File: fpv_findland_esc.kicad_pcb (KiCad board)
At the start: 6 copper layers, 36 x 47.4 mm, 157 parts, among them J1 Conn_01x01_Pin, J10 Conn_01x01_Pin, J11 Conn_01x01_Pin, J12 Conn_01x01_Pin, J13 Conn_01x06, J2 Conn_01x01_Pin, J3 Conn_01x01_Pin, J4 Conn_01x01_Pin, J5 Conn_01x01_Pin, J6 Conn_01x01_Pin, J7 Conn_01x01_Pin, J8 Conn_01x01_Pin, J9 Conn_01x01_Pin, Q1 FDMC8010DC, Q10 FDMC8010DC, Q11 FDMC8010DC, Q12 FDMC8010DC, Q13 FDMC8010DC, Q14 FDMC8010DC, Q15 FDMC8010DC, Q16 FDMC8010DC, Q17 FDMC8010DC, Q18 FDMC8010DC, Q19 FDMC8010DC, Q2 FDMC8010DC, Q20 FDMC8010DC, Q21 FDMC8010DC, Q22 FDMC8010DC, Q23 FDMC8010DC, Q24 FDMC8010DC, Q3 FDMC8010DC, Q4 FDMC8010DC, Q5 FDMC8010DC, Q6 FDMC8010DC, Q7 FDMC8010DC, Q8 FDMC8010DC, Q9 FDMC8010DC, U1 GD32E230G8U6, U11 WL2851E33, U2 DRV8300D, U3 GD32E230G8U6, U4 DRV8300D, U5 GD32E230G8U6, U6 DRV8300D, U7 GD32E230G8U6, U8 DRV8300D, U9 ST732M50R

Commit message: Fixed revisions
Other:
- board text added: "${revision}"

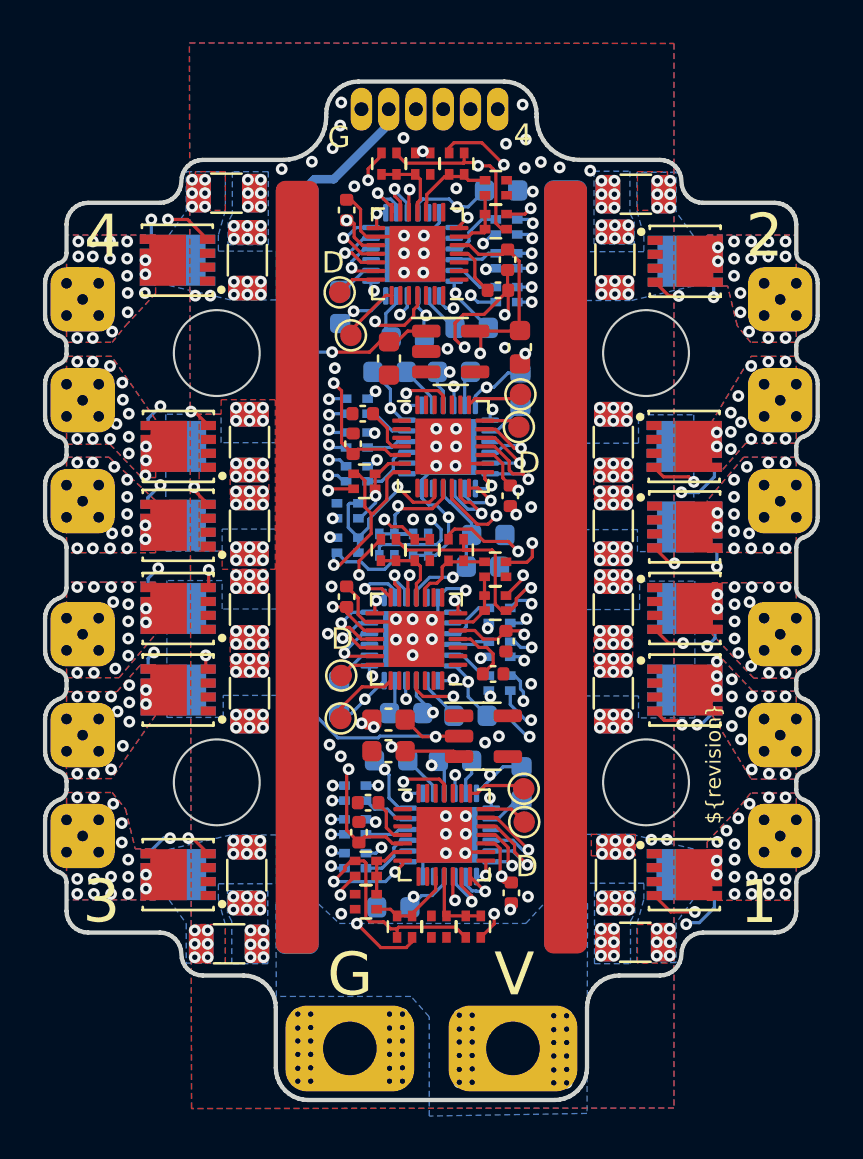
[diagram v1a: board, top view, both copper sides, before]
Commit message: Added copperfill for VBAT in layer In4. Other small fixes.
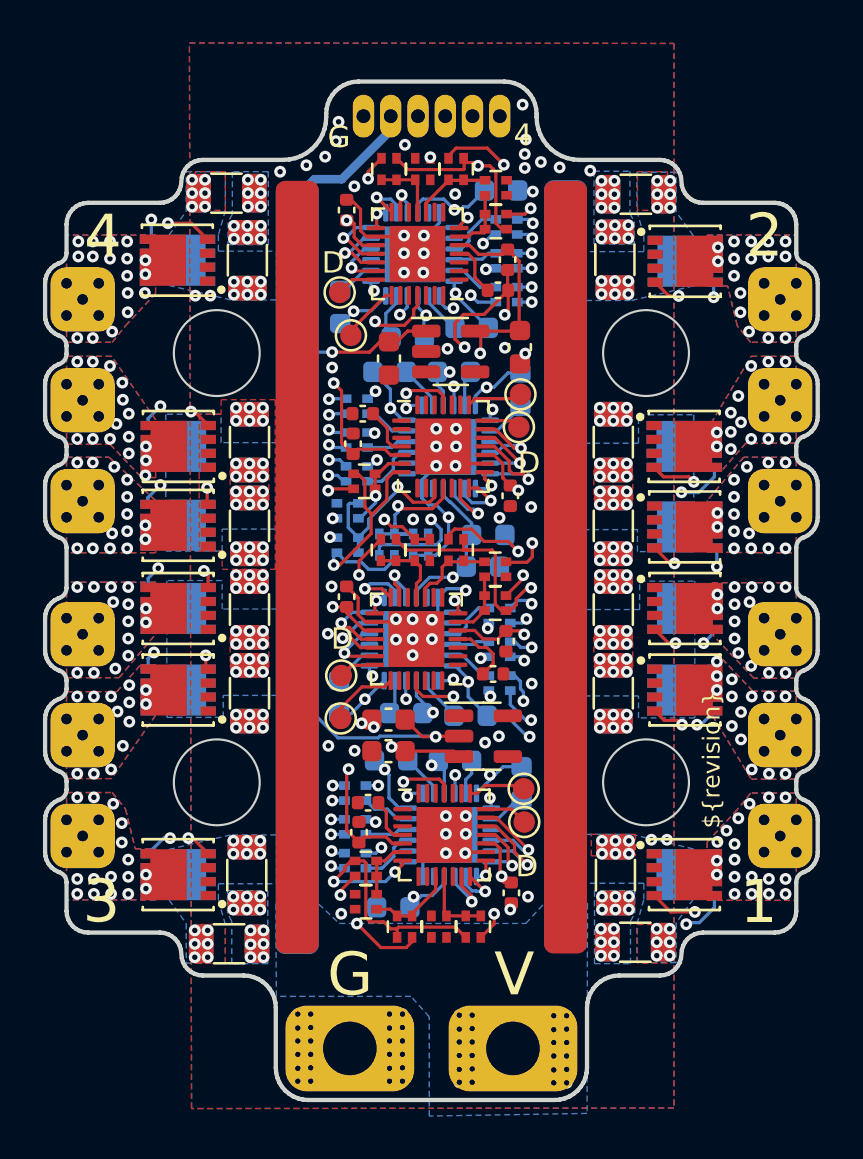
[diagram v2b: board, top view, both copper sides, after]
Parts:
- moved J13 0.34 mm to (138.7, 54.0)
- moved RN24 0.25 mm to (136.7, 56.4)
- moved RN20 0.25 mm to (133.5, 56.4)
- moved RN21 0.25 mm to (135.1, 56.4)
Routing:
- net /VBAT: track 79.7 -> 90.8 mm
- net /Motor2/V_SENSE: track 3.24 -> 0.00 mm, vias 1 -> 0
- net /3.3V: track 99.9 -> 102.8 mm
- net /Motor1/V_SENSE: track 1.15 -> 0.00 mm, vias 1 -> 0
- net /Motor4/V_SENSE: track 1.08 -> 0.00 mm, vias 1 -> 0
- net /Motor3/V_SENSE: track 1.07 -> 0.00 mm, vias 1 -> 0
- net /Motor3/CLOW: track 2.55 -> 1.76 mm
- net Net-(Q24-G): track 10.6 -> 9.89 mm
- added copper zone on In2.Cu, net /VBAT

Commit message: Optimized layer In2 for more current.
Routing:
- net /5V: track 75.2 -> 73.8 mm
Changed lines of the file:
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@@
   (via (at 133.646479 83.347485) (size 0.55) (drill 0.25) (layers "F.Cu" "B.Cu") (net 196))
   (segment (start 136.042746 91.7) (end 139.438173 91.7) (width 0.3) (layer "In2.Cu") (net 196))
-  (segment (start 136.4995 75.45) (end 137.425 75.45) (width 0.3) (layer "In2.Cu") (net 196))
+  (segment (start 140.85 73.125) (end 140.85 71.957107) (width 0.3) (layer "In2.Cu") (net 196))
+  (segment (start 140.85 64.25) (end 140.85 71.957107) (width 0.3) (layer "In2.Cu") (net 196))
   (segment (start 140.594655 90.543518) (end 140.594655 84.021695) (width 0.3) (layer "In2.Cu") (net 196))
   (segment (start 135.9149 83.80102) (end 140.37398 83.80102) (width 0.3) (layer "In2.Cu") (net 196))
-  (segment (start 141.325 73.125) (end 141.325 71.482107) (width 0.3) (layer "In2.Cu") (net 196))
   (segment (start 135.733375 83.633375) (end 135.747255 83.633375) (width 0.3) (layer "In2.Cu") (net 196))
+  (segment (start 137.425 75.45) (end 139.75 73.125) (width 0.3) (layer "In2.Cu") (net 196))
   (segment (start 135.747255 83.633375) (end 135.9149 83.80102) (width 0.3) (layer "In2.Cu") (net 196))
+  (segment (start 138.314228 58.114228) (end 139.5 59.3) (width 0.3) (layer "In2.Cu") (net 196))
+  (segment (start 139.5 59.3) (end 139.5 62.9) (width 0.3) (layer "In2.Cu") (net 196))
   (segment (start 136.954592 58.114228) (end 138.314228 58.114228) (width 0.3) (layer "In2.Cu") (net 196))
-  (segment (start 139.75 73.125) (end 141.325 73.125) (width 0.3) (layer "In2.Cu") (net 196))
-  (segment (start 137.425 75.45) (end 139.75 73.125) (width 0.3) (layer "In2.Cu") (net 196))
   (segment (start 140.594655 84.021695) (end 140.37398 83.80102) (width 0.3) (layer "In2.Cu") (net 196))
-  (segment (start 139.5 59.3) (end 139.5 62.9) (width 0.3) (layer "In2.Cu") (net 196))
   (segment (start 134.668246 90.3255) (end 136.042746 91.7) (width 0.3) (layer "In2.Cu") (net 196))
   (segment (start 136.74382 58.325) (end 136.954592 58.114228) (width 0.3) (layer "In2.Cu") (net 196))
-  (segment (start 141.325 71.482107) (end 141.325 82.85) (width 0.3) (layer "In2.Cu") (net 196))
-  (segment (start 141.325 64.725) (end 141.325 71.482107) (width 0.3) (layer "In2.Cu") (net 196))
+  (segment (start 136.5745 58.325) (end 136.74382 58.325) (width 0.3) (layer "In2.Cu") (net 196))
   (segment (start 133.748994 83.45) (end 135.55 83.45) (width 0.3) (layer "In2.Cu") (net 196))
-  (segment (start 139.5 62.9) (end 141.325 64.725) (width 0.3) (layer "In2.Cu") (net 196))
+  (segment (start 139.75 73.125) (end 140.85 73.125) (width 0.3) (layer "In2.Cu") (net 196))
   (segment (start 133.646479 83.347485) (end 133.748994 83.45) (width 0.3) (layer "In2.Cu") (net 196))
-  (segment (start 141.325 82.85) (end 140.37398 83.80102) (width 0.3) (layer "In2.Cu") (net 196))
+  (segment (start 136.4995 75.45) (end 137.425 75.45) (width 0.3) (layer "In2.Cu") (net 196))
+  (segment (start 139.5 62.9) (end 140.85 64.25) (width 0.3) (layer "In2.Cu") (net 196))
+  (segment (start 140.85 83.325) (end 140.37398 83.80102) (width 0.3) (layer "In2.Cu") (net 196))
   (segment (start 135.55 83.45) (end 135.733375 83.633375) (width 0.3) (layer "In2.Cu") (net 196))
-  (segment (start 136.5745 58.325) (end 136.74382 58.325) (width 0.3) (layer "In2.Cu") (net 196))
-  (segment (start 138.314228 58.114228) (end 139.5 59.3) (width 0.3) (layer "In2.Cu") (net 196))
+  (segment (start 140.85 71.957107) (end 140.85 83.325) (width 0.3) (layer "In2.Cu") (net 196))
   (segment (start 139.438173 91.7) (end 140.594655 90.543518) (width 0.3) (layer "In2.Cu") (net 196))
   (segment (start 137.375 72.925) (end 137.375 73.475) (width 0.15) (layer "B.Cu") (net 196))

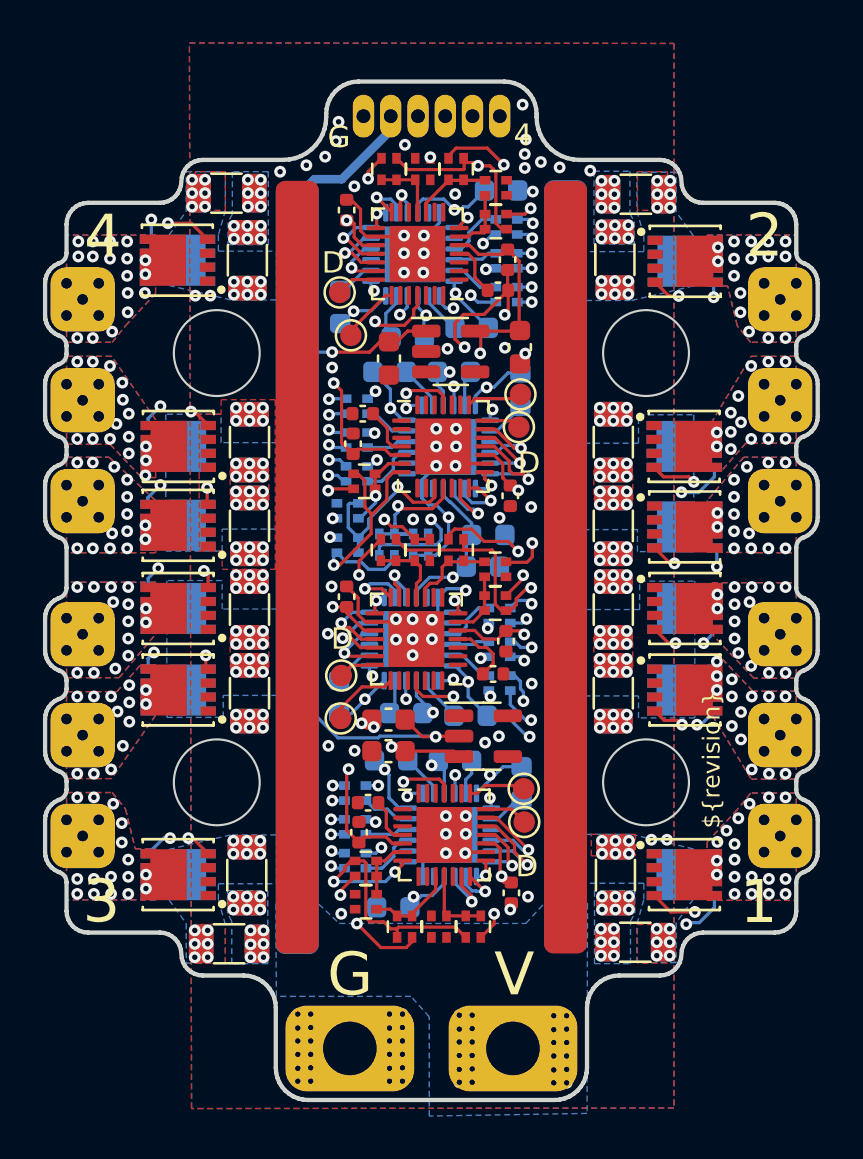
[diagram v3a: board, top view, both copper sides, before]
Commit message: Moved top layer fets to allow more current. Other small improvements.
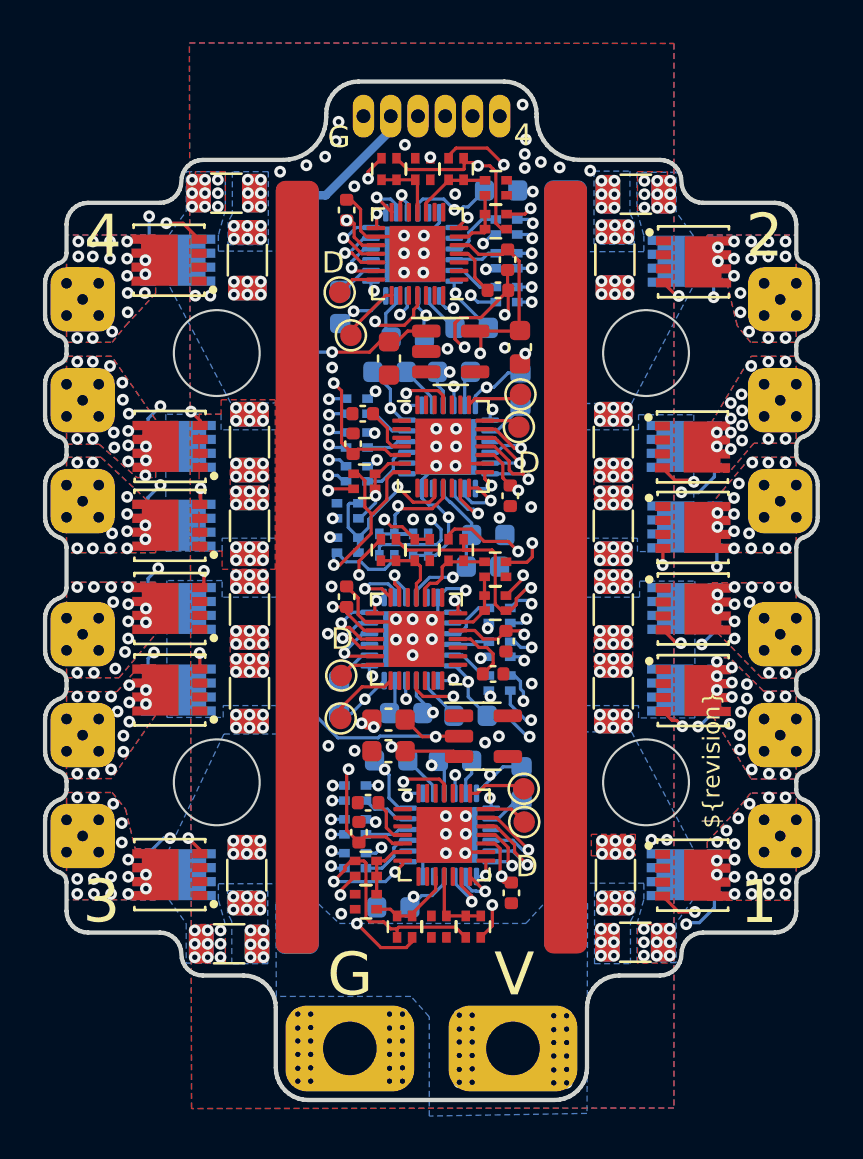
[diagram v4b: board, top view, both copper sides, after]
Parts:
- moved Q12 0.39 mm to (147.7, 89.3)
- moved Q2 0.39 mm to (147.7, 60.8)
- moved Q10 0.39 mm to (147.7, 69.4)
- moved Q7 0.39 mm to (147.7, 73.1)
- moved Q8 0.39 mm to (147.7, 76.9)
- moved Q9 0.39 mm to (147.7, 80.7)
- moved Q11 0.39 mm to (123.3, 89.3)
- moved Q3 0.39 mm to (123.3, 73.0)
- moved Q4 0.39 mm to (123.3, 69.3)
- moved Q5 0.39 mm to (123.3, 80.7)
- moved Q6 0.39 mm to (123.3, 76.9)
- moved Q1 0.39 mm to (123.3, 60.7)
- renumbered C40 to C1, C57 to C10, C64 to C11, C22 to C12, C5 to C13, C4 to C14, C23 to C15, C58 to C16, C30 to C17, C31 to C18, C25 to C19, C38 to C2, C8 to C20, C13 to C21, C29 to C22, C6 to C23, C49 to C24, C50 to C25, C48 to C26, C43 to C27, C1 to C28, C51 to C29, C15 to C3, C53 to C30, C55 to C31, C52 to C32, C69 to C33, C70 to C34, C37 to C35, C19 to C36, C39 to C37, C17 to C38, C45 to C39, C18 to C4, C47 to C40, C46 to C41, C44 to C42, C61 to C43, C60 to C44, C3 to C45, C20 to C46, C62 to C47, C10 to C48, C9 to C49, C16 to C5, C27 to C50, C14 to C51, C7 to C52, C59 to C53, C12 to C54, C26 to C55, C21 to C56, C2 to C57, C28 to C58, C24 to C59, C71 to C6, C66 to C60, C54 to C61, C11 to C62, C67 to C63, C65 to C64, C68 to C7, C63 to C8, C32 to C9, J4 to J1, J8 to J10, J12 to J11, J10 to J12, J11 to J13, J13 to J2, J9 to J3, J6 to J4, J3 to J5, J5 to J6, J1 to J7, J2 to J8, J7 to J9, Q8 to Q1, Q16 to Q10, Q6 to Q11, Q20 to Q12, Q17 to Q13, Q7 to Q14, Q23 to Q15, Q15 to Q16, Q13 to Q17, Q21 to Q18, Q11 to Q19, Q18 to Q2, Q9 to Q20, Q2 to Q21, Q3 to Q22, Q19 to Q23, Q5 to Q24, Q12 to Q3, Q10 to Q4, Q4 to Q5, Q1 to Q6, Q14 to Q7, Q24 to Q8, Q22 to Q9, RN24 to RN1, RN29 to RN10, RN31 to RN11, RN8 to RN12, RN4 to RN13, RN6 to RN14, RN5 to RN15, RN7 to RN16, RN19 to RN17, RN17 to RN19, RN23 to RN2, RN16 to RN20, RN25 to RN21, RN15 to RN22, RN10 to RN23, RN13 to RN24, RN12 to RN25, RN9 to RN26, RN2 to RN27, RN26 to RN28, RN11 to RN29, RN21 to RN3, RN1 to RN30, RN3 to RN31, RN27 to RN32, RN20 to RN4, RN22 to RN5, RN14 to RN6, RN28 to RN7, RN30 to RN8, RN32 to RN9, TP5 to TP1, TP2 to TP10, TP13 to TP11, TP14 to TP12, TP9 to TP13, TP10 to TP14, TP3 to TP2, TP6 to TP3, TP11 to TP4, TP8 to TP5, TP4 to TP6, TP1 to TP8, TP12 to TP9, U5 to U1, U4 to U10, U11 to U2, U1 to U3, U7 to U4, U9 to U5, U3 to U6, U6 to U7, U2 to U9
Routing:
- net /Motor1/MotorOutC: track 34.3 -> 35.5 mm
- net /Motor3/MotorOutA: track 38.2 -> 37.2 mm
- net /5V: track 73.8 -> 73.0 mm
- net Net-(Q14-G): track 18.6 -> 17.8 mm
- net /Motor3/MotorOutC: track 35.0 -> 34.4 mm
- net /VBAT: track 90.8 -> 90.6 mm, vias 122 -> 134
- net /Motor2/MotorOutB: track 27.6 -> 27.7 mm, vias 17 -> 18
- net /Motor4/MotorOutB: track 32.6 -> 32.5 mm, vias 16 -> 19
- net /Motor2/MotorOutC: vias 16 -> 14
- net GND: vias 189 -> 187
- net /Motor4/MotorOutC: vias 17 -> 15
- net /Motor3/MotorOutB: vias 16 -> 18
- net /Motor1/MotorOutB: vias 15 -> 16

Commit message: Moved motor pads to allow more current.
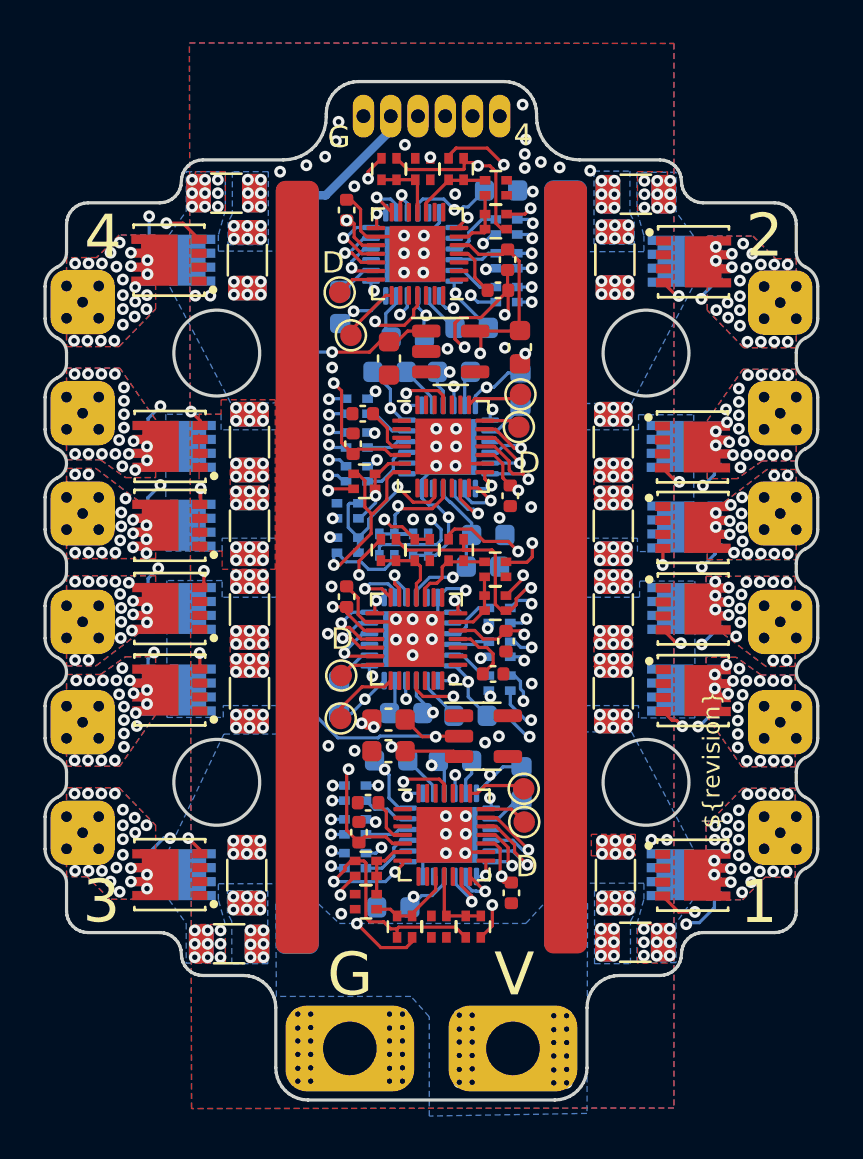
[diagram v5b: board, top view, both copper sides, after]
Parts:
- moved J10 0.60 mm to (151.8, 67.8)
- moved J13 0.60 mm to (151.8, 82.2)
- moved J6 0.60 mm to (119.2, 67.8)
- moved J8 0.60 mm to (119.2, 82.2)
- moved J11 0.57 mm to (151.8, 77.5)
- moved J4 0.57 mm to (119.2, 72.5)
- moved J7 0.57 mm to (119.2, 77.5)
- moved J9 0.57 mm to (151.8, 72.5)
- moved J12 0.15 mm to (151.8, 87.3)
- moved J5 0.15 mm to (119.2, 87.3)
- moved J3 0.15 mm to (151.8, 62.6)
- moved J1 0.12 mm to (119.2, 62.6)
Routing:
- net Net-(Q16-G): track 17.9 -> 16.6 mm
- net /Motor1/MotorOutB: track 30.1 -> 28.9 mm, vias 16 -> 22
- net /Motor2/MotorOutB: track 27.7 -> 26.6 mm, vias 18 -> 21
- net /Motor2/MotorOutC: track 29.5 -> 29.1 mm, vias 14 -> 18
- net /Motor2/MotorOutA: track 33.3 -> 32.9 mm, vias 19 -> 25
- net /Motor1/MotorOutA: track 36.5 -> 36.1 mm, vias 16 -> 18
- net /Motor4/MotorOutC: vias 15 -> 19
- net /Motor4/MotorOutB: vias 19 -> 21
- net /Motor4/MotorOutA: vias 20 -> 25
- net /Motor3/MotorOutC: vias 18 -> 23
- net /Motor3/MotorOutB: vias 18 -> 23
- net /Motor3/MotorOutA: vias 16 -> 18
- net /Motor1/MotorOutC: vias 18 -> 23
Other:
- outline, holes or cut-outs redrawn
